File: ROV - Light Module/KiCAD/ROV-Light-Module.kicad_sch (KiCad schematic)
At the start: 29 parts, among them J4 Conn_02x05_Odd_Even, J7 Bottom - Middle, J8 Middle - Top, J9 Middle - Top, U1 AL8805W5

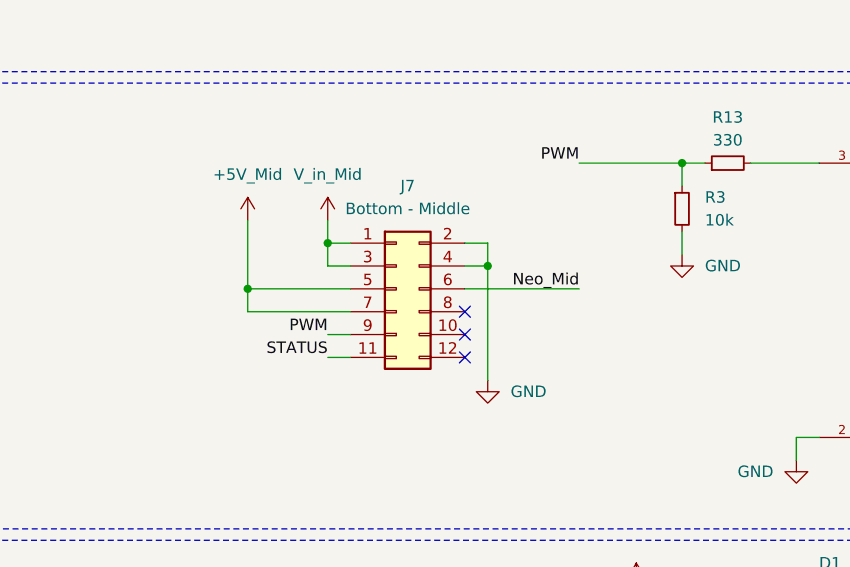
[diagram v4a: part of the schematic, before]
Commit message: change header to match
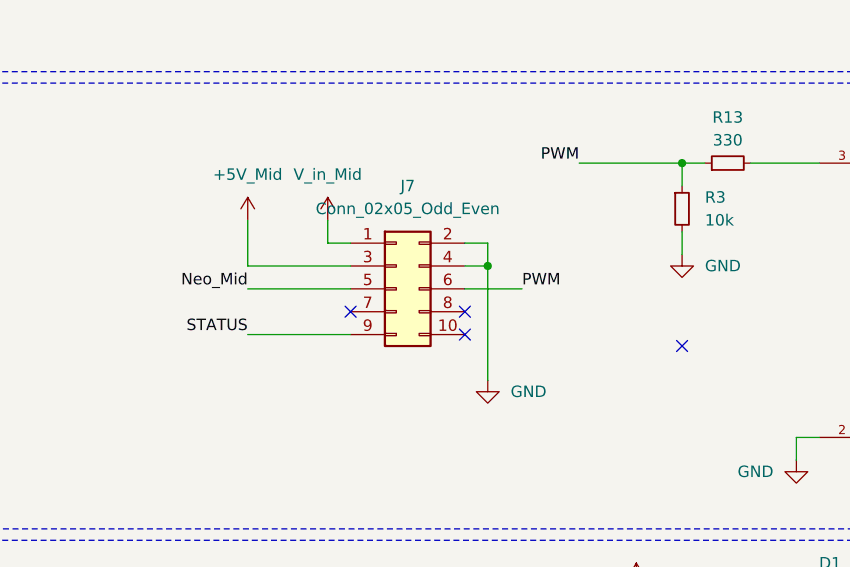
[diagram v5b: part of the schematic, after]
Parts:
- J7: value Bottom - Middle -> Conn_02x05_Odd_Even; footprint Connector_PinHeader_1.27mm:PinHeader_2x06_P1.27mm_Vertical_SMD -> Connector_PinHeader_1.27mm:PinHeader_2x05_P1.27mm_Vertical_SMD; symbol Connector_Generic:Conn_02x06_Odd_Even -> Connector_Generic:Conn_02x05_Odd_Even
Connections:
- net +5V_Mid: now also J7.3 (Pin_3); no longer J7.5 (Pin_5), J7.7 (Pin_7)
- net Neo_Mid: now also J7.5 (Pin_5); no longer J7.6 (Pin_6)
- net PWM: now also J7.6 (Pin_6); no longer J7.9 (Pin_9)
- net STATUS: now also J7.9 (Pin_9); no longer J7.11 (Pin_11)
- net V_in_Mid: no longer J7.3 (Pin_3)
- no-connect marks 5 -> 6
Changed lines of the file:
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@@
 	)
 	(junction
-		(at 36.83 120.65)
-		(diameter 0)
-		(color 0 0 0 0)
-	)
-	(junction
 		(at 153.67 106.68)
 		(diameter 0)
@@
 	)
 	(junction
-		(at 45.72 115.57)
-		(diameter 0)
-		(color 0 0 0 0)
-	)
-	(junction
 		(at 153.67 116.84)
 		(diameter 0)
@@
 	)
 	(no_connect
-		(at 60.96 128.27)
+		(at 60.96 123.19)
 	)
 	(no_connect
-		(at 60.96 123.19)
+		(at 48.26 123.19)
 	)
 	(no_connect
@@
 	)
 	(no_connect
+		(at 85.09 127)
+	)
+	(no_connect
 		(at 60.96 125.73)
 	)
@@
 	(wire
 		(pts
-			(xy 36.83 123.19) (xy 36.83 120.65)
-		)
-		(stroke
-			(width 0)
-			(type default)
-		)
-	)
-	(wire
-		(pts
 			(xy 138.43 106.68) (xy 138.43 109.22)
 		)
@@
 	(wire
 		(pts
-			(xy 60.96 120.65) (xy 73.66 120.65)
-		)
-		(stroke
-			(width 0)
-			(type default)
-		)
-	)
-	(wire
-		(pts
 			(xy 92.71 106.68) (xy 100.33 106.68)
 		)
@@
 	(wire
 		(pts
-			(xy 36.83 120.65) (xy 48.26 120.65)
-		)
-		(stroke
-			(width 0)
-			(type default)
-		)
-	)
-	(wire
-		(pts
 			(xy 95.25 59.69) (xy 104.14 59.69)
 		)
@@
 	(wire
 		(pts
-			(xy 36.83 123.19) (xy 48.26 123.19)
-		)
-		(stroke
-			(width 0)
-			(type default)
-		)
-	)
-	(wire
-		(pts
 			(xy 77.47 160.02) (xy 99.06 160.02)
 		)
@@
 	(wire
 		(pts
-			(xy 45.72 128.27) (xy 48.26 128.27)
-		)
-		(stroke
-			(width 0)
-			(type default)
-		)
-	)
-	(wire
-		(pts
 			(xy 116.84 54.61) (xy 119.38 54.61)
 		)
@@
 	(wire
 		(pts
-			(xy 36.83 113.03) (xy 36.83 120.65)
+			(xy 36.83 113.03) (xy 36.83 118.11)
 		)
 		(stroke
@@
 	(wire
 		(pts
+			(xy 60.96 120.65) (xy 67.31 120.65)
+		)
+		(stroke
+			(width 0)
+			(type default)
+		)
+	)
+	(wire
+		(pts
 			(xy 135.89 170.18) (xy 135.89 181.61)
 		)
@@
 	(wire
 		(pts
+			(xy 36.83 120.65) (xy 48.26 120.65)
+		)
+		(stroke
+			(width 0)
+			(type default)
+		)
+	)
+	(wire
+		(pts
 			(xy 77.47 29.21) (xy 80.01 29.21)
 		)
@@
 	(wire
 		(pts
-			(xy 45.72 118.11) (xy 48.26 118.11)
+			(xy 77.47 39.37) (xy 80.01 39.37)
 		)
 		(stroke
@@
 	(wire
 		(pts
-			(xy 77.47 39.37) (xy 80.01 39.37)
+			(xy 36.83 118.11) (xy 48.26 118.11)
 		)
 		(stroke
@@
 	(wire
 		(pts
-			(xy 45.72 125.73) (xy 48.26 125.73)
+			(xy 36.83 125.73) (xy 48.26 125.73)
 		)
 		(stroke
@@
 	(wire
 		(pts
-			(xy 45.72 115.57) (xy 45.72 118.11)
-		)
-		(stroke
-			(width 0)
-			(type default)
-		)
-	)
-	(wire
-		(pts
 			(xy 135.89 162.56) (xy 135.89 165.1)
 		)
@@
 	)
 	(label "Neo_Mid"
-		(at 73.66 120.65 180)
+		(at 36.83 120.65 180)
 		(effects
 			(font
@@
 	)
 	(label "STATUS"
-		(at 45.72 128.27 180)
+		(at 36.83 125.73 180)
 		(effects
 			(font
@@
 	)
 	(label "PWM"
-		(at 45.72 125.73 180)
+		(at 67.31 120.65 0)
 		(effects
 			(font
 				(size 1.27 1.27)
 			)
-			(justify right bottom)
+			(justify left bottom)
 		)
 	)
@@
 			(justify left bottom)
 		)
-		(property "Net Class" "1 oz - 1 A"
+		(property "Netclass" "1 oz - 1 A"
 			(at 133.9799 115.84 0)
 			(show_name no)
@@
 			(justify left bottom)
 		)
-		(property "Net Class" "PCBway min 1 oz "
+		(property "Netclass" "PCBway min 1 oz "
 			(at 34.9199 178.07 0)
 			(show_name no)
@@
 			(justify left bottom)
 		)
-		(property "Net Class" "PCBway min 1 oz "
+		(property "Netclass" "PCBway min 1 oz "
 			(at 78.0999 185.69 0)
 			(show_name no)
@@
 			(justify left bottom)
 		)
-		(property "Net Class" "1 oz - 1 A"
+		(property "Netclass" "1 oz - 1 A"
 			(at 149.2199 126 0)
 			(show_name no)
@@
 			(justify left bottom)
 		)
-		(property "Net Class" "1 oz - 1 A"
+		(property "Netclass" "1 oz - 1 A"
 			(at 47.6199 114.57 0)
 			(show_name no)
@@
 			(justify left bottom)
 		)
-		(property "Net Class" "PCBway min 1 oz "
+		(property "Netclass" "PCBway min 1 oz "
 			(at 102.2299 185.69 0)
 			(show_name no)
@@
 			(justify left bottom)
 		)
-		(property "Net Class" "PCBway min 1 oz "
+		(property "Netclass" "PCBway min 1 oz "
 			(at 95.8799 105.68 0)
 			(show_name no)
@@
 		(length 1)
 		(shape round)
-		(at 38.1 120.65 0)
+		(at 38.1 118.11 0)
 		(fields_autoplaced yes)
 		(effects
@@
 			(justify left bottom)
 		)
-		(property "Net Class" "1 oz - 1 A"
-			(at 38.7299 119.65 0)
+		(property "Netclass" "1 oz - 1 A"
+			(at 38.7299 117.11 0)
 			(show_name no)
 			(do_not_autoplace no)
@@
 		)
 		(property "Component Class" ""
-			(at -207.01 92.71 0)
+			(at -207.01 90.17 0)
 			(show_name no)
 			(do_not_autoplace no)
@@
 			(justify left bottom)
 		)
-		(property "Net Class" "PCBway min 1 oz "
+		(property "Netclass" "PCBway min 1 oz "
 			(at 53.9699 185.69 0)
 			(show_name no)
@@
 			(justify left bottom)
 		)
-		(property "Net Class" "PCBway min 1 oz "
+		(property "Netclass" "PCBway min 1 oz "
 			(at 139.0599 180.61 0)
 			(show_name no)
@@
 			(justify left bottom)
 		)
-		(property "Net Class" "PCBway min 1 oz "
+		(property "Netclass" "PCBway min 1 oz "
 			(at 75.5599 105.68 0)
 			(show_name no)
@@
 			(justify left bottom)
 		)
-		(property "Net Class" "1 oz - 1 A"
+		(property "Netclass" "1 oz - 1 A"
 			(at 62.8599 114.57 0)
 			(show_name no)
@@
 			(justify left bottom)
 		)
-		(property "Net Class" "1 oz - 1 A"
+		(property "Netclass" "1 oz - 1 A"
 			(at 88.2599 161.56 0)
 			(show_name no)
@@
 			(justify left bottom)
 		)
-		(property "Net Class" "1 oz - 1 A"
+		(property "Netclass" "1 oz - 1 A"
 			(at 93.3399 159.02 0)
 			(show_name no)
@@
 			(justify left bottom)
 		)
-		(property "Net Class" "PCBway min 1 oz "
+		(property "Netclass" "PCBway min 1 oz "
 			(at 160.6499 170.45 0)
 			(show_name no)
@@
 			(justify left bottom)
 		)
-		(property "Net Class" "PCBway min 1 oz "
+		(property "Netclass" "PCBway min 1 oz "
 			(at 97.1499 61.23 0)
 			(show_name no)
@@
 			(justify left bottom)
 		)
-		(property "Net Class" "PCBway min 1 oz "
+		(property "Netclass" "PCBway min 1 oz "
 			(at 198.7499 126 0)
 			(show_name no)
@@
 			(justify left bottom)
 		)
-		(property "Net Class" "1 oz - 1 A"
+		(property "Netclass" "1 oz - 1 A"
 			(at 130.1699 136.16 0)
 			(show_name no)
@@
 			(justify left bottom)
 		)
-		(property "Net Class" "PCBway min 1 oz "
+		(property "Netclass" "PCBway min 1 oz "
 			(at 36.1899 161.56 0)
 			(show_name no)
@@
 			(justify left bottom)
 		)
-		(property "Net Class" "PCBway min 1 oz "
+		(property "Netclass" "PCBway min 1 oz "
 			(at 97.1499 58.69 0)
 			(show_name no)
@@
 			(justify left bottom)
 		)
-		(property "Net Class" "1 oz - 2 A"
+		(property "Netclass" "1 oz - 2 A"
 			(at 79.3699 164.1 0)
 			(show_name no)
@@
 			(justify left bottom)
 		)
-		(property "Net Class" "PCBway min 1 oz "
+		(property "Netclass" "PCBway min 1 oz "
 			(at 198.7499 123.46 0)
 			(show_name no)
@@
 	)
 	(symbol
-		(lib_id "Connector_Generic:Conn_02x06_Odd_Even")
+		(lib_id "Connector_Generic:Conn_02x05_Odd_Even")
 		(at 53.34 120.65 0)
 		(unit 1)
@@
 			)
 		)
-		(property "Value" "Bottom - Middle"
+		(property "Value" "Conn_02x05_Odd_Even"
 			(at 54.61 111.76 0)
 			(show_name no)
@@
 			)
 		)
-		(property "Footprint" "Connector_PinHeader_1.27mm:PinHeader_2x06_P1.27mm_Vertical_SMD"
+		(property "Footprint" "Connector_PinHeader_1.27mm:PinHeader_2x05_P1.27mm_Vertical_SMD"
 			(at 53.34 120.65 0)
 			(hide yes)
@@
 			)
 		)
-		(property "Description" "Generic connector, double row, 02x06, odd/even pin numbering scheme (row 1 odd numbers, row 2 even numbers), script generated (kicad-library-utils/schlib/autogen/connector/)"
+		(property "Description" "Generic connector, double row, 02x05, odd/even pin numbering scheme (row 1 odd numbers, row 2 even numbers), script generated (kicad-library-utils/schlib/autogen/connector/)"
 			(at 53.34 120.65 0)
 			(hide yes)
@@
 		(pin "9"
 		)
-		(pin "11"
-		)
-		(pin "12"
-		)
 		(instances

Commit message: massive cleanup
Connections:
- no-connect marks 6 -> 5

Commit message: .
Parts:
- added R15: 4k7, Resistor_SMD:R_0805_2012Metric_Pad1.20x1.40mm_HandSolder, symbol Device:R_Small
- added R16, R17, R18: 470, Resistor_SMD:R_0805_2012Metric_Pad1.20x1.40mm_HandSolder, symbol Device:R_Small
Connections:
- net +5V: now also R15.1, R18.1
- net GND: now also R16.2, R17.2
- new net Function: R15.2, R16.1, R17.1, R18.2
- no-connect marks 5 -> 4

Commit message: clean up schematics
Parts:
- J4: value Conn_02x05_Odd_Even -> Conn_02x06_Odd_Even; footprint Connector_PinSocket_1.27mm:PinSocket_2x05_P1.27mm_Vertical_SMD -> Connector_PinSocket_1.27mm:PinSocket_2x06_P1.27mm_Vertical_SMD; symbol Connector_Generic:Conn_02x05_Odd_Even -> Connector_Generic:Conn_02x06_Odd_Even
- J7: value Conn_02x05_Odd_Even -> Conn_02x06_Odd_Even; footprint Connector_PinHeader_1.27mm:PinHeader_2x05_P1.27mm_Vertical_SMD -> Connector_PinHeader_1.27mm:PinHeader_2x06_P1.27mm_Vertical_SMD; symbol Connector_Generic:Conn_02x05_Odd_Even -> Connector_Generic:Conn_02x06_Odd_Even
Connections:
- net +5V: now also J4.5 (Pin_5); no longer J4.3 (Pin_3), R15.1, R18.1
- net +5V_Mid: now also R15.1, R18.1
- net A9/D9: now also J4.9 (Pin_9); no longer J4.7 (Pin_7)
- net Function: now also J4.12 (Pin_12); no longer R15.2, R16.1, R17.1, R18.2
- net NeoPixle: now also J4.7 (Pin_7); no longer J4.5 (Pin_5)
- net STATUS: now also J7.11 (Pin_11); no longer J7.9 (Pin_9)
- net STATUS_LED: now also J4.11 (Pin_11); no longer J4.9 (Pin_9)
- net Neopixle_Mid: now reaches J7.7 (Pin_7)
- net Neopixle_Mid: now also J8.3 (Pin_3)
- net Function_Mid: now reaches J7.8 (Pin_8)
- net Function_Mid: now also R15.2, R16.1, R17.1, R18.2
- net Neo_Mid: no longer names the net of J7.5 (Pin_5)
- net Neo_Mid: no longer J8.3 (Pin_3)
- new net V_Supply: J4.3 (Pin_3)
- no-connect marks 4 -> 6
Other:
- moved on the sheet: R15, R16, R17, R18
